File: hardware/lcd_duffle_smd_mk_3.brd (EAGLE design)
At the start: 80 x 36 mm, 15 parts, among them IC1 ATTINY84, IC2 WS2811

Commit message: wooo
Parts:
- removed AVRISP: AVR_SPI_PRG_6SMD-M-RA, A_butts:1X06-SMD
- removed D2: MBRA140, A_butts:SMA-DIODE
- removed I2C: I2C, A_butts:1X04-SMD
- added JP1: M06SMD, A_butts:1X06-SMD
- added MONOCHROME?: JUMPER-PAD-2-NOYES_SILK, A_butts:PAD-JUMPER-2-NO_YES_SILK
- moved R2 20.7 mm to (38.0, 15.5), turned to 270 degrees
- moved D1 19.9 mm to (43.5, 16.0)
- moved R3 12.1 mm to (43.5, 19.5), turned to 180 degrees
- moved R1 2.92 mm to (35.5, 15.5)
- moved IC1 2.69 mm to (35.5, 22.0)
- moved C3 2.12 mm to (43.5, 24.5), turned to 0 degrees
- moved C1 1.80 mm to (33.0, 15.5), turned to 270 degrees
- moved R4 1.80 mm to (43.5, 22.0), turned to 180 degrees
- moved C2 1.00 mm to (15.9, 18.0)
- moved CONTRAST 1.00 mm to (12.4, 17.9)
- moved IC2 1.00 mm to (49.5, 22.0)
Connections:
- removed net LED_CNTL: AVRISP.1, IC1.8, IC2.6
- removed net N$3: AVRISP.2, D2.C
- new net LIGHT: IC1.6, IC2.6, MONOCHROME?.2
- new net MISO: IC1.8, JP1.2
- net 5V: no longer D2.A
- net E: now also IC1.5; no longer IC1.6
- net GND: now also JP1.6; no longer AVRISP.6, I2C.1, U$1.10, U$1.7, U$1.8, U$1.9
- net N$1: now also JP1.5; no longer I2C.4
- net R: now also MONOCHROME?.1
- net RESET: now also JP1.1; no longer AVRISP.5
- net RS: now also IC1.2; no longer IC1.3
- net RW: now also IC1.3; no longer IC1.5
- net SCL: now also JP1.4; no longer AVRISP.3, I2C.2
- net SDA: now also JP1.3; no longer AVRISP.4, I2C.3
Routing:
- net RESET: track 0.00 -> 40.1 mm, vias 0 -> 2
- net 5V: track 100.7 -> 62.4 mm, vias 1 -> 2
- net MISO: track 0.00 -> 35.7 mm, vias 0 -> 2
- net CONTRAST: track 27.2 -> 0.00 mm
- net SDA: track 10.4 -> 36.9 mm, vias 0 -> 2
- net E: track 0.00 -> 25.6 mm
- net RW: track 0.00 -> 24.7 mm
- net SCL: track 14.0 -> 37.1 mm, vias 0 -> 3
- net N$1: track 3.51 -> 25.3 mm
- net LIGHT: track 0.00 -> 20.1 mm
- net R: track 19.8 -> 25.5 mm
- net RS: track 29.6 -> 24.9 mm
- net N$3: track 3.39 -> 0.00 mm
- net DB7: track 8.33 -> 10.4 mm
- net DB6: track 7.81 -> 9.84 mm
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
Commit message: ready for the fab
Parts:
- added R5: (no value), A_butts:R0805
- added U$2, U$3: (no value), A_butts:COW
- added U$4, U$5: (no value), A_butts:CC-BY-SA-4.0-NO-URL
- added U$6: (no value), A_butts:OSHWLOGO_TOP_0.2_A
- added U$7: (no value), A_butts:OSHWLOGO_BOT_0.2_A
- CONTRAST: device A_butts:POT-THUMBWHEEL -> A_butts:RTRIM3314Z-SIDE
- moved CONTRAST 11.3 mm to (3.86, 25.4)
- moved C2 6.61 mm to (11.5, 22.9), turned to 180 degrees
- moved C1 2.83 mm to (30.7, 17.2), turned to 0 degrees
- moved R2 1.31 mm to (39.3, 15.5)
- moved D1 1.20 mm to (44.7, 16.0)
- moved MONOCHROME? 0.35 mm to (45.6, 28.0)
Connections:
- net CONTRAST: now also R5.1; no longer CONTRAST.2@1
- net GND: now also R5.2
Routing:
- net 5V: track 62.4 -> 90.7 mm, vias 2 -> 3
- net CONTRAST: track 0.00 -> 14.3 mm
- net E: track 25.6 -> 22.9 mm
- net R: track 25.5 -> 23.1 mm
- net SCL: track 37.1 -> 35.1 mm
- net RW: track 24.7 -> 22.9 mm
- net N$1: track 25.3 -> 24.1 mm
- net RS: track 24.9 -> 24.2 mm
- net G: track 20.2 -> 19.5 mm
- net B: track 19.4 -> 18.7 mm
- net SDA: track 36.9 -> 36.3 mm
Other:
- board text added: "1-2K <- Permanently Set Contrast"
- board text added: "GND"
- board text added: "LCD Dufflebag (Like a backpack, but derpier) by schizobovine <sean@yak.net>"
- board text added: "MISO"
- board text added: "MOSI/SDA"
- board text added: "RST"
- board text added: "SCK/SCL"
- board text added: "VCC"
- board text added: "Version 3.0 (SMD)"

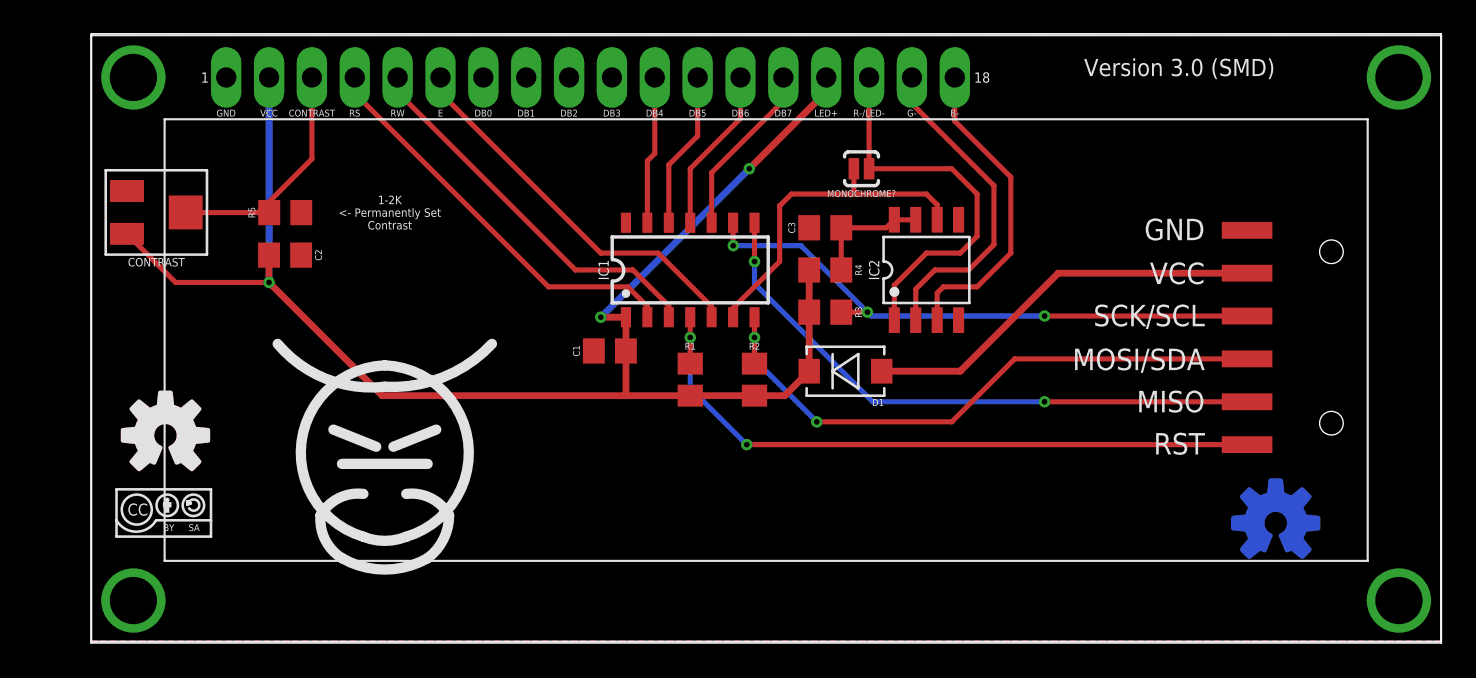
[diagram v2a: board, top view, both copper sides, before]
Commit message: minor tweaks to stop overlapping silkscreen
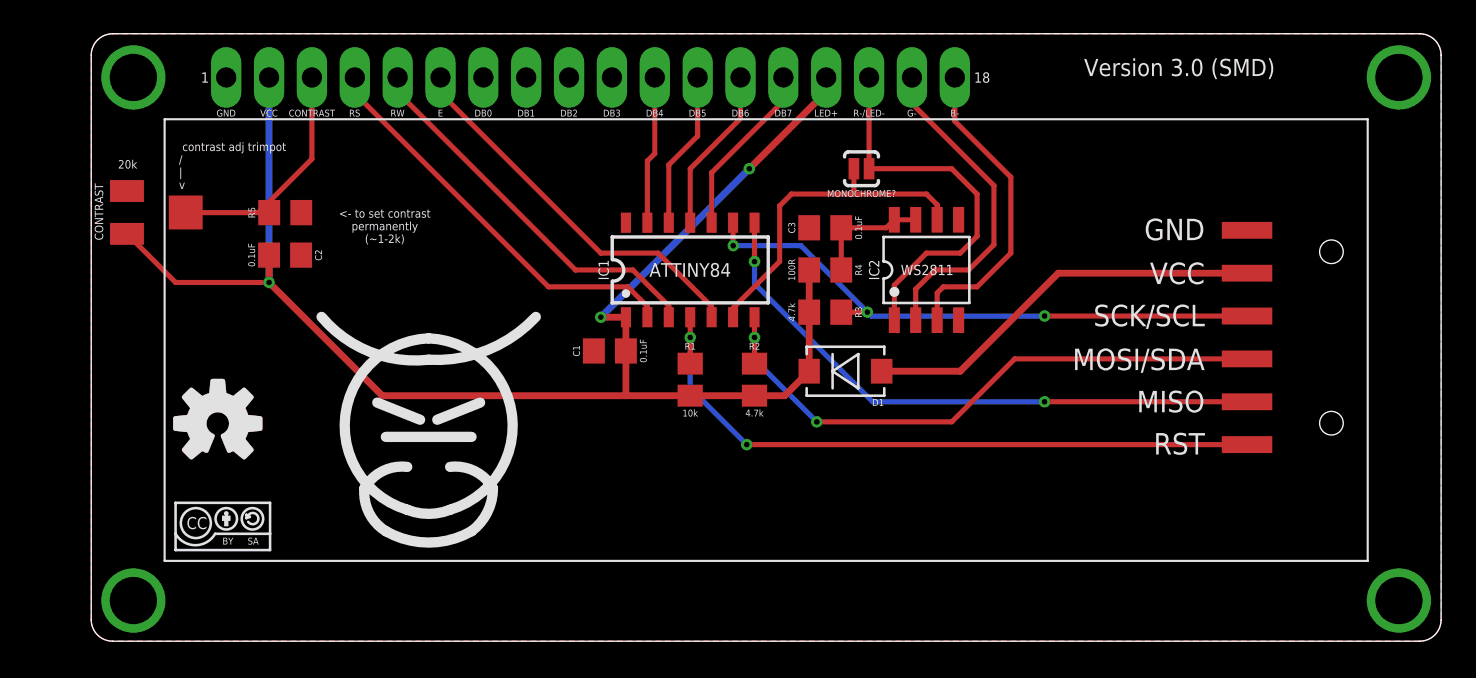
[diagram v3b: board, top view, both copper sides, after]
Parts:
- moved U$5 68.5 mm to (7.80, 6.80)
- moved U$7 63.0 mm to (7.50, 12.9)
- moved U$4 3.59 mm to (7.80, 6.80)
- moved U$6 3.18 mm to (7.50, 12.9)
- moved U$2 3.05 mm to (20.0, 11.6)
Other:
- outline, holes or cut-outs redrawn
- board text added: "<- to set contrast permanently (~1-2k)"
- board text added: "LCD Dufflebag SMD Mark III (Like a backpack, but punnier) by schizobovine <sean@yak.net>"
- board text added: "contrast adj trimpot / | v"
- board text removed: "1-2K <- Permanently Set Contrast"
- board text removed: "LCD Dufflebag (Like a backpack, but derpier) by schizobovine <sean@yak.net>"
